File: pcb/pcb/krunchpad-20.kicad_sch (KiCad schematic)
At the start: 42 parts, among them J1 Conn_01x04_Socket, SW1 SW_Push_45deg, SW10 SW_Push_45deg, SW11 SW_Push_45deg, SW12 SW_Push_45deg, SW13 SW_Push_45deg, SW14 SW_Push_45deg, SW15 SW_Push_45deg, SW16 SW_Push_45deg, SW17 SW_Push_45deg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

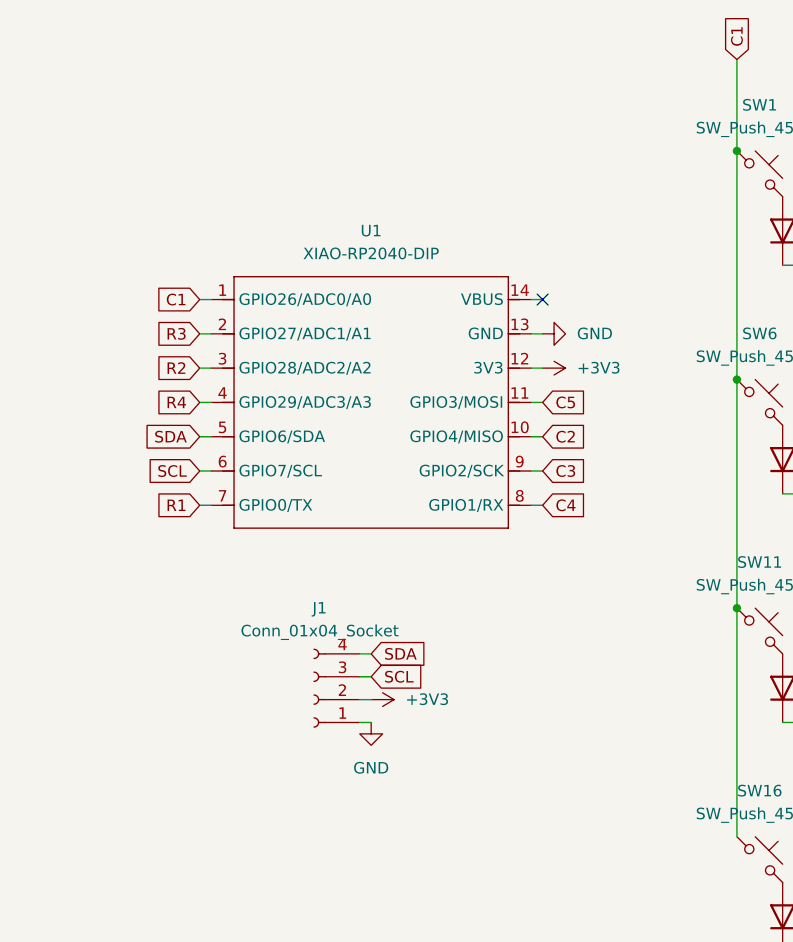
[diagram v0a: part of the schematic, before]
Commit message: Changed oled socket to SMD, added extra slot for 128x64 oled, updated relevent info info in BOM, updated images
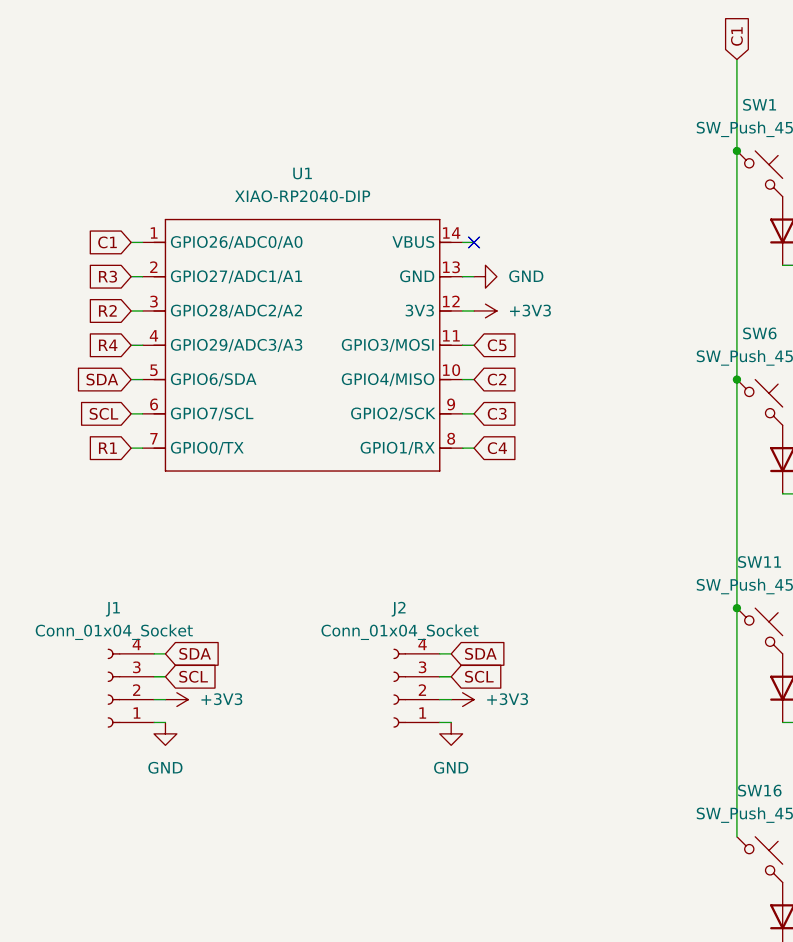
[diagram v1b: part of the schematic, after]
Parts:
- added J2: Conn_01x04_Socket, Connector_PinSocket_2.54mm:PinSocket_1x04_P2.54mm_Vertical_SMD_Pin1Left, symbol Connector:Conn_01x04_Socket
- J1: footprint 0.91-OLED:SSD1306-0.91-OLED-4pin-128x32 -> Connector_PinSocket_2.54mm:PinSocket_1x04_P2.54mm_Vertical_SMD_Pin1Left
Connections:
- net +3V3: now also J2.2 (Pin_2)
- net GND: now also J2.1 (Pin_1)
- net SCL: now also J2.3 (Pin_3)
- net SDA: now also J2.4 (Pin_4)
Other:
- moved on the sheet: J1, U1

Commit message: updated pcb file with rotary encoder, updated gerber and case
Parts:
- added JP1, JP2: SolderJumper_2_Bridged, Jumper:SolderJumper-2_P1.3mm_Bridged_RoundedPad1.0x1.5mm, symbol Jumper:SolderJumper_2_Bridged
- added SW21: RotaryEncoder_Switch, Rotary_Encoder:RotaryEncoder_Alps_EC11E-Switch_Vertical_H20mm, symbol Device:RotaryEncoder_Switch
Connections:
- net GND: now also SW21.C
- net SCL renamed GP7/SCL
- net GP7/SCL: now also JP2.2 (B)
- net SDA renamed GP6/SDA
- net GP6/SDA: now also JP1.1 (A)
- new net: JP2.1 (A), SW21.B
- new net: JP1.2 (B), SW21.A
- no-connect marks 1 -> 3
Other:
- moved on the sheet: J1, J2, U1
